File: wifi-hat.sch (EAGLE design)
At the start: 16 parts

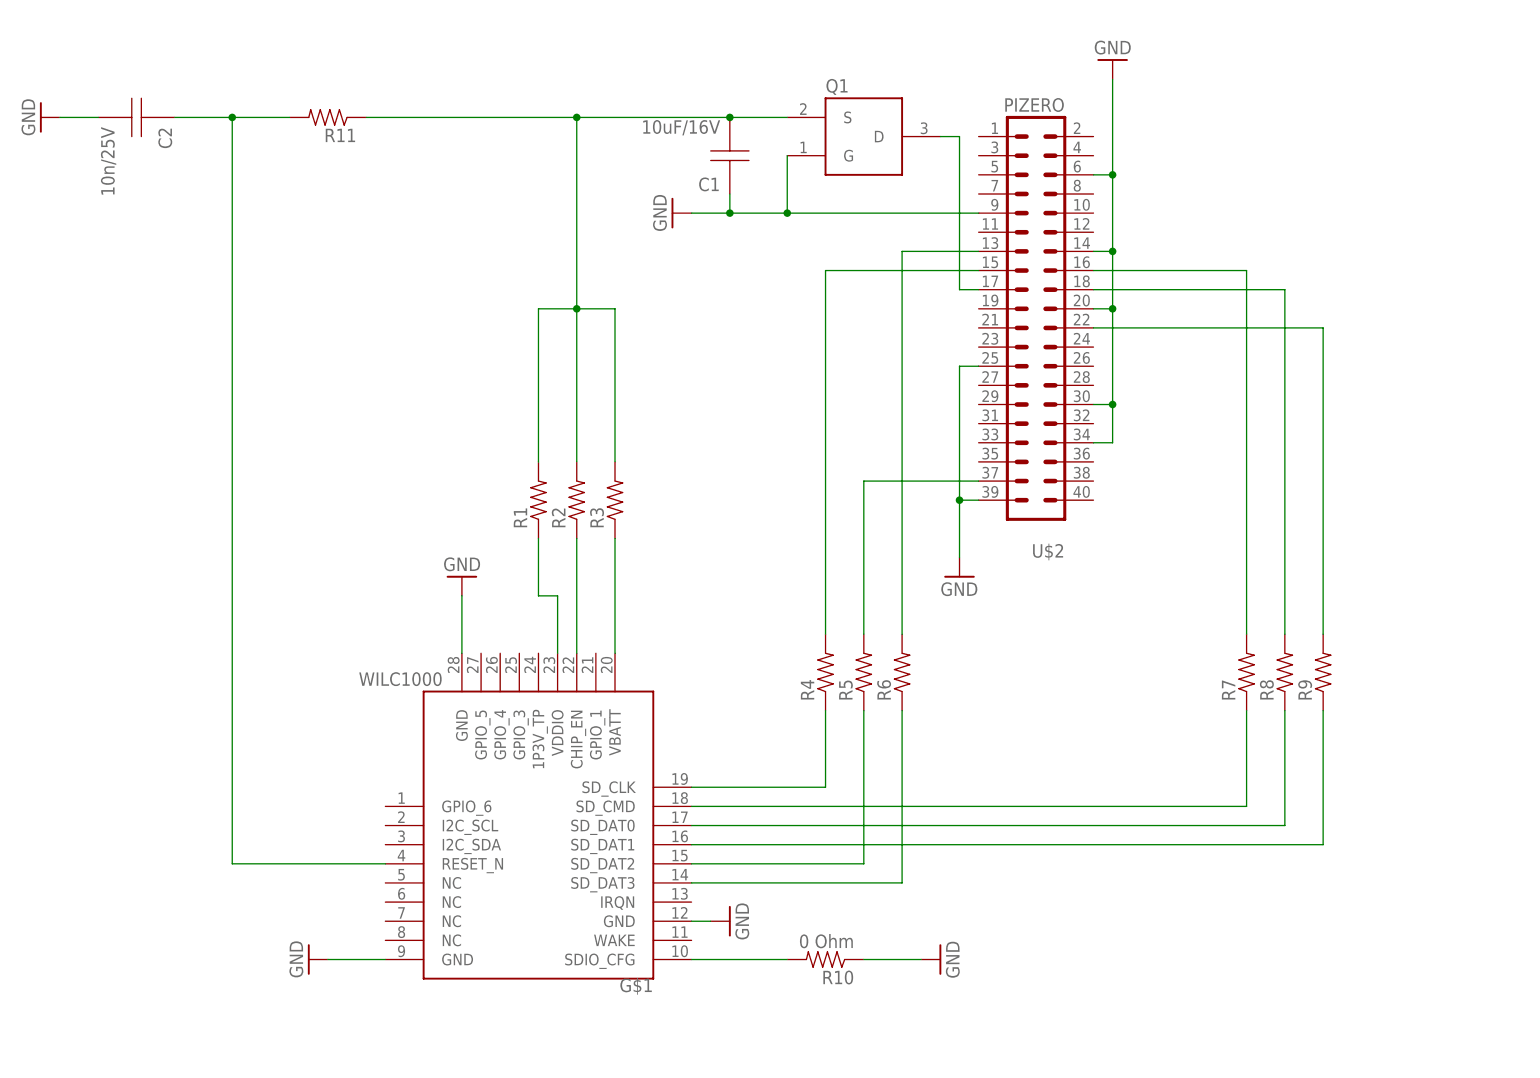
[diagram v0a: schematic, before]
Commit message: cleanup and fixes
Cleaned up the board and schematic layouts. Connected RESET_N to GPIO to handle power cycling.
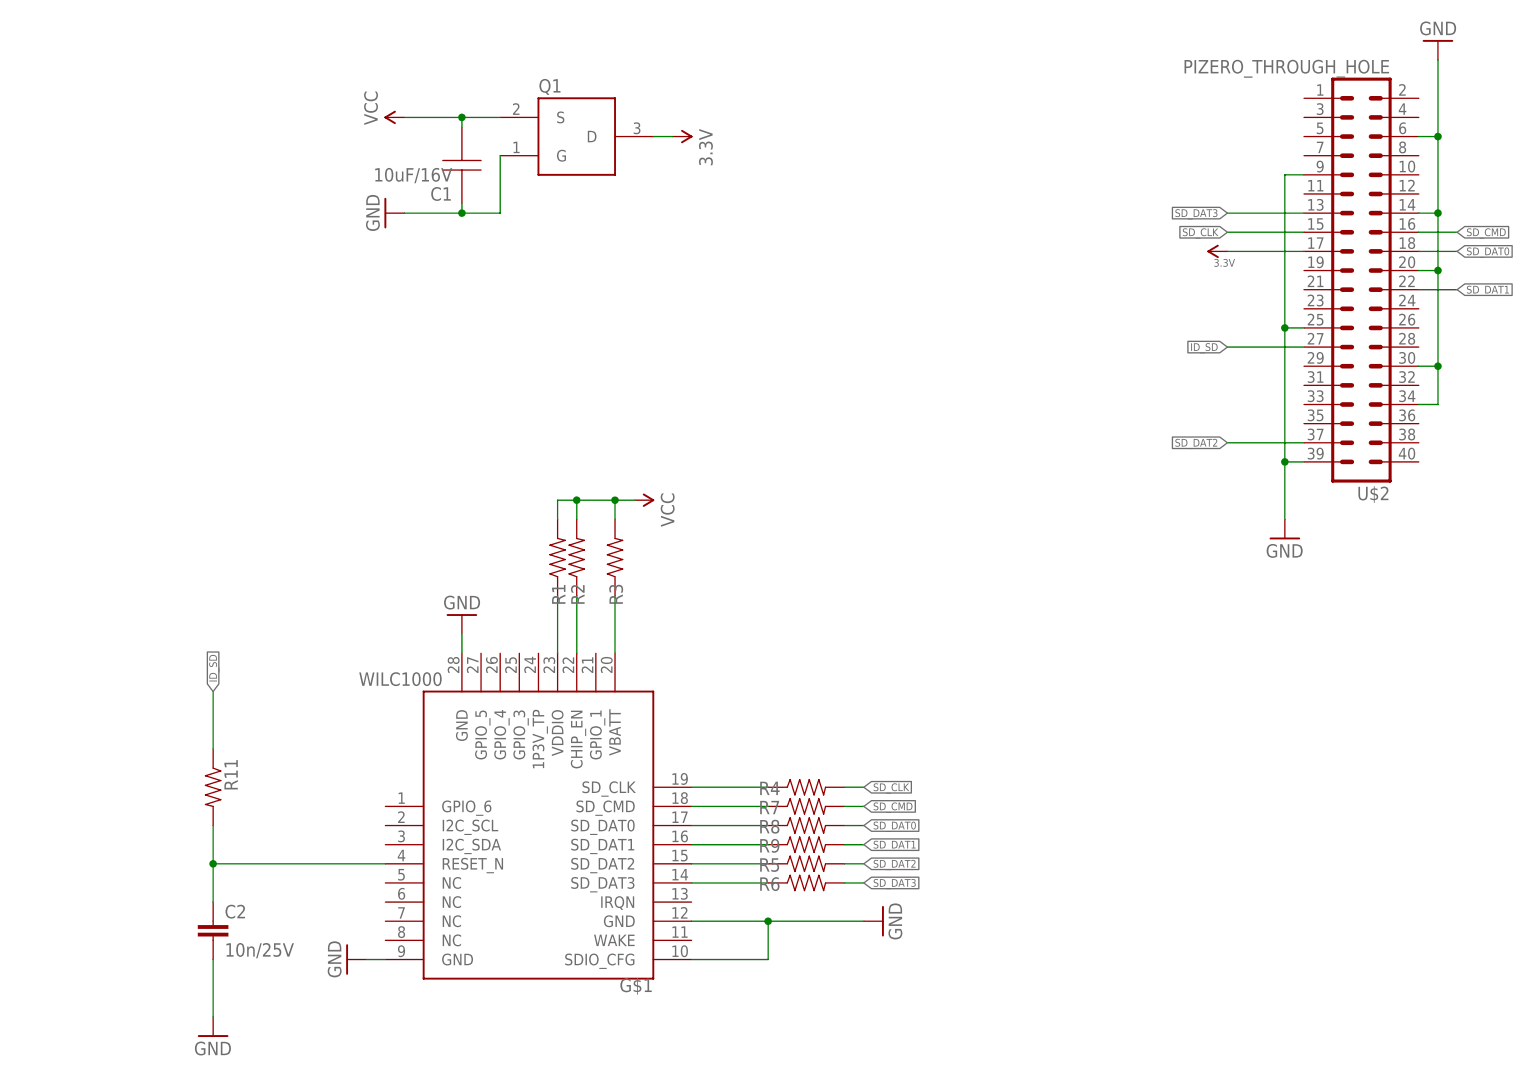
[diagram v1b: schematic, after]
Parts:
- removed R10: 0 Ohm, SparkFun-Resistors:RESISTOR0603-RES
- C2: device sym:CAP -> resistor:C-EUC0603K
- U$2: value PIZERO -> PIZERO_THROUGH_HOLE
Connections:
- net 3V3 renamed 3.3V
- net N$11 renamed SD_DAT2
- net N$12 renamed SD_CMD
- net N$13 renamed SD_DAT0
- net N$14 renamed SD_DAT1
- net R6 renamed SD_DAT3
- removed net N$9: C2.A, R11.2, U$1.RESET_N
- removed net S$2: R4.2, U$2.15
- removed net SDIO_CFG: R10.2, U$1.SDIO_CFG
- new net ID_SD: R11.1, U$2.27
- new net N$23: R4.1, U$1.SD_CLK
- new net RESET_N: C2.1, R11.2, U$1.RESET_N
- net GND: now also C2.2, U$1.SDIO_CFG; no longer C2.B, R10.1
- net SD_CLK: now also R4.2, U$2.15; no longer R4.1, U$1.SD_CLK
- net VCC: no longer R11.1
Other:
- moved on the sheet: C1, Q1, R1, R11, R2, R3, R4, R5, R6, R7, R8, R9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

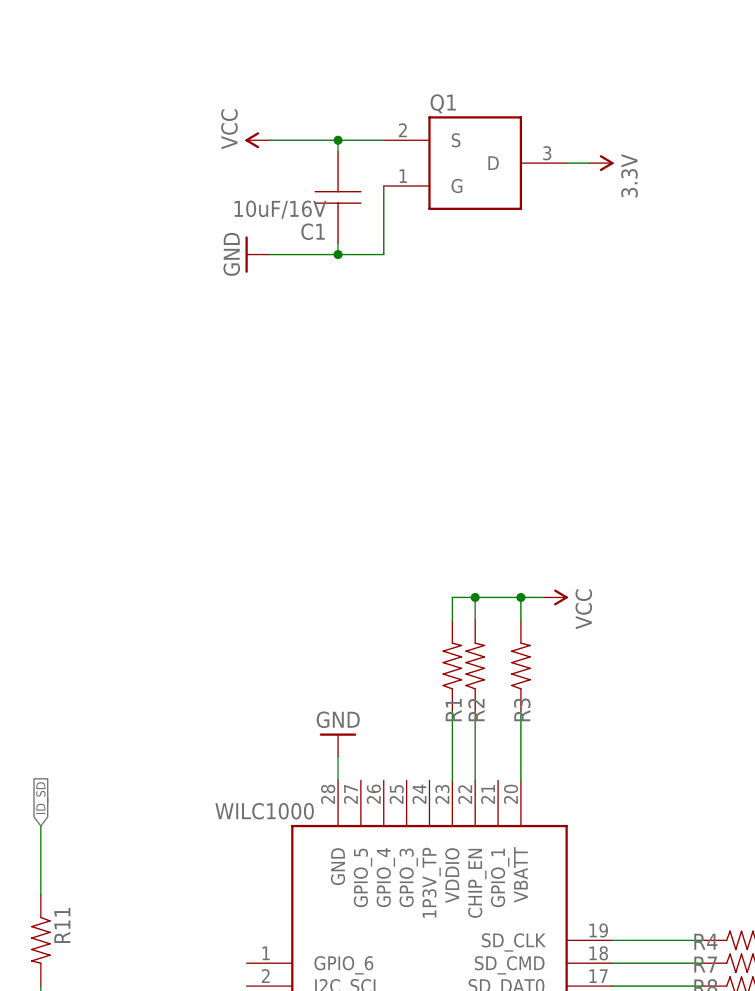
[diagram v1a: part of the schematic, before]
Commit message: Replace Caps with 603 variants
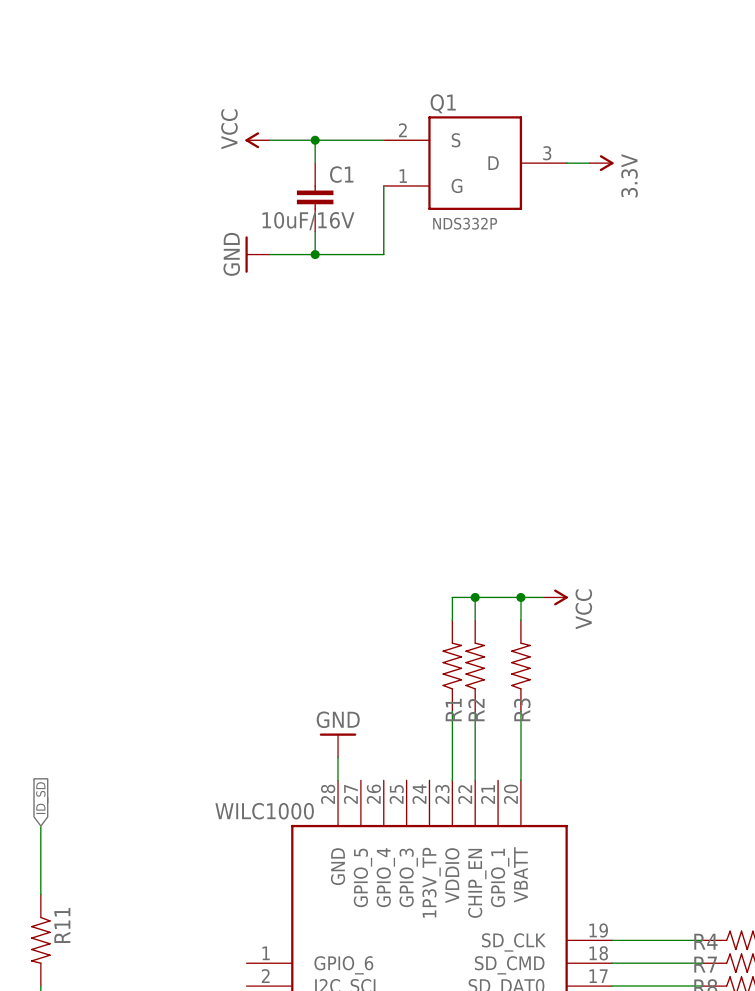
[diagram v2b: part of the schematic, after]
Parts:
- C1: device sym:CAP -> resistor:C-EUC0603K
- Q1: value (none) -> NDS332P
- renumbered U$1 to WI_SOC
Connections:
- net GND: now also C1.2; no longer C1.A
- net VCC: now also C1.1; no longer C1.B
